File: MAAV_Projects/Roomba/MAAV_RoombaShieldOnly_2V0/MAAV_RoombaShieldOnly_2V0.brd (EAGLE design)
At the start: 53.3 x 59.7 mm, 16 parts, among them U2 ARDUINO_SHIELDLABEL

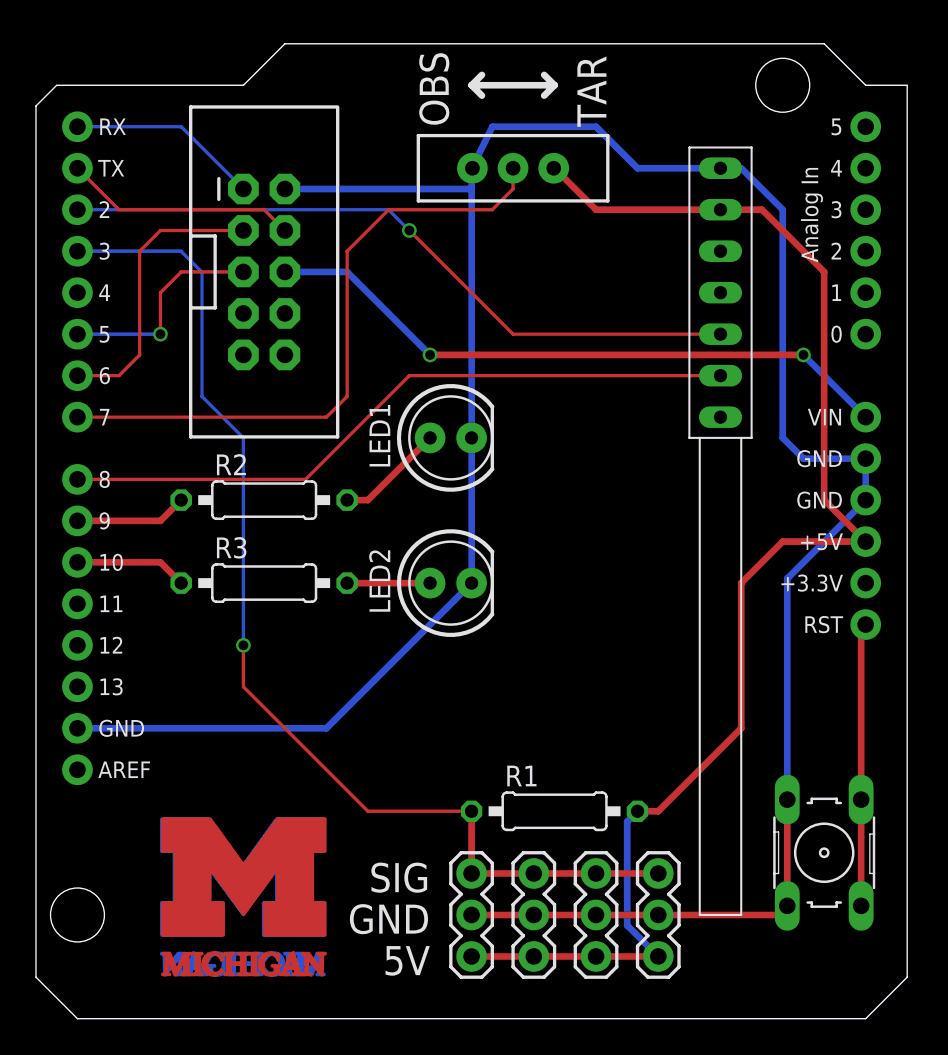
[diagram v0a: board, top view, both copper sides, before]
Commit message: moved some files around and added SMD version of roomba shiled
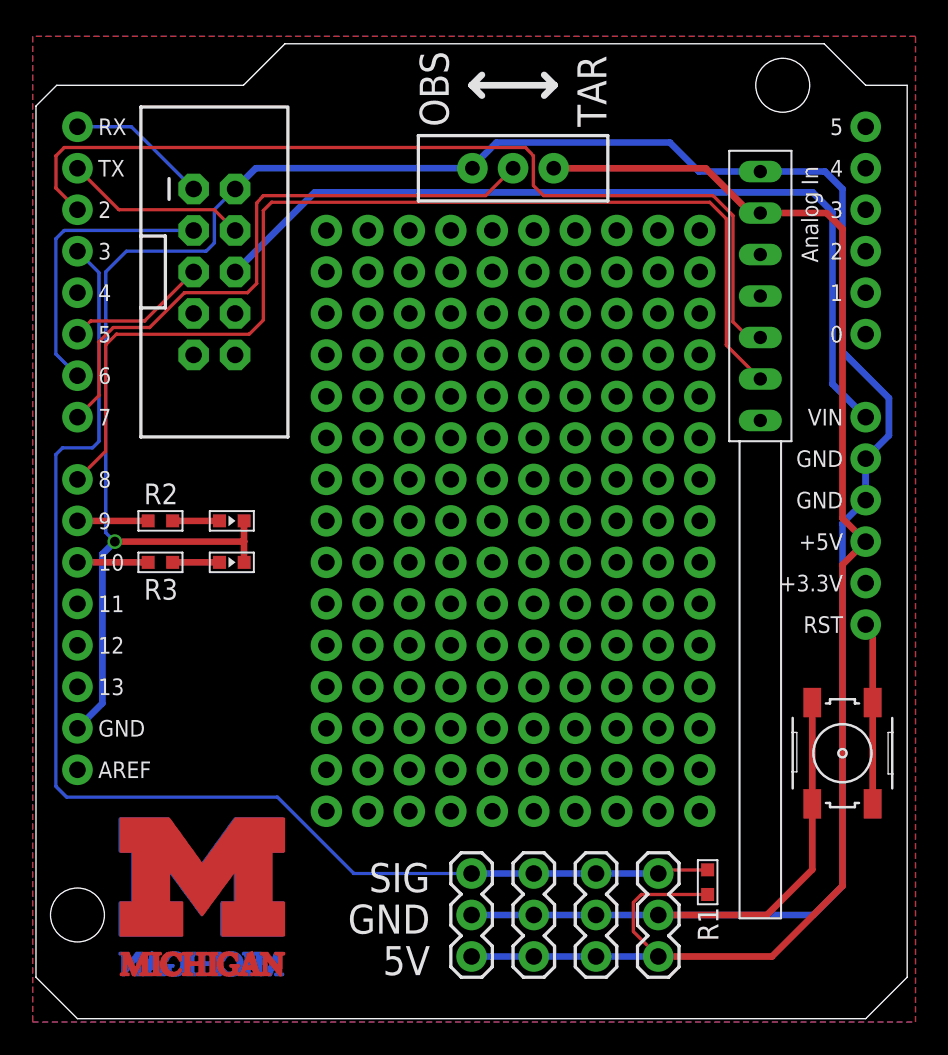
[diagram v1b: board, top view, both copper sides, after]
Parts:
- LED1, LED2: device SparkFun:LED5MM -> Jon_LIB:CHIPLED_0603
- R1, R2, R3: device rcl:0207/10 -> Jon_LIB:R0603
- S2: value TACT_BUTTON_THRU-HOLE -> TACT_BUTTON_SMD; device MAAV_Roomba:SIMPLE_BUTTON -> MAAV_Roomba:SIMPLE_BUTTON_SMD
- moved LED1 14.3 mm to (12.0, 30.5)
- moved LED2 13.5 mm to (12.0, 27.9)
- moved R1 10.3 mm to (41.1, 8.36), turned to 270 degrees
- moved R2 6.48 mm to (7.62, 30.5)
- moved R3 6.48 mm to (7.62, 27.9)
- moved S2 6.20 mm to (49.4, 16.3), turned to 270 degrees
- moved JP1 3.05 mm to (10.9, 45.7)
- moved U$12 2.54 mm to (10.2, 6.35)
- moved U$13 2.54 mm to (10.2, 6.35)
- moved SV1 2.45 mm to (44.3, 44.2)
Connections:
- net GND: now also LED1.C, LED2.C, S2.P$3, S2.P$4; no longer LED1.K, LED2.K, S2.1, S2.2
- net RESET: now also S2.P$1, S2.P$2; no longer S2.3, S2.4
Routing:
- net GND: track 155.9 -> 179.8 mm, vias 0 -> 1
- net RF_D3: track 42.0 -> 65.6 mm
- net RF_D2: track 42.5 -> 56.9 mm, vias 1 -> 0
- net VIN: track 39.2 -> 52.5 mm, vias 2 -> 0
- net HALL_BUS: track 67.0 -> 77.7 mm, vias 1 -> 0
- net 5V: track 84.2 -> 93.8 mm
- net RESET: track 17.3 -> 11.2 mm
- net CREATE_PWR_TOG: track 13.2 -> 8.69 mm, vias 1 -> 0
- net N$1: track 6.66 -> 2.87 mm
- net CREATE_TX: track 11.7 -> 8.69 mm
- net CREATE_RX: track 14.3 -> 11.2 mm
- net LED_RED: track 6.88 -> 4.33 mm
- net LED_GREEN: track 6.88 -> 4.33 mm
- net N$2: track 5.08 -> 2.87 mm
- net SWITCH_1: track 38.9 -> 37.8 mm
- added copper zone on layer 1, net GND
- added copper zone on layer 16, net GND
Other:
- board text added: "Brian Leu"
- board text added: "Date:"
- board text added: "Designed by:"
- board text added: "Jason Leung"
- board text added: "Jonathan Kurzer"
- board text added: "Matthew Sauvé"
- board text added: "May 2014"
- board text added: "Michigan Autonomous Aerial Vehicles"
- board text added: "University of Michigan"
- board text removed: "Designed by: Date:"
- board text removed: "Jonathan Kurzer May 2014"
- board text removed: "University of Michigan Michigan Autonomous Aerial Vehicles"
